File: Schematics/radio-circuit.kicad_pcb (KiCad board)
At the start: 4 copper layers, 58 x 32 mm, 40 parts, among them J1 USB_B_Micro, J2 STDC14, J3 0, U1 USBLC6-2SC6, U2 LD39015M33R, U3 STM32F042C6T6, U4 Si4705-D60-GM, Y1 SG-3030CM

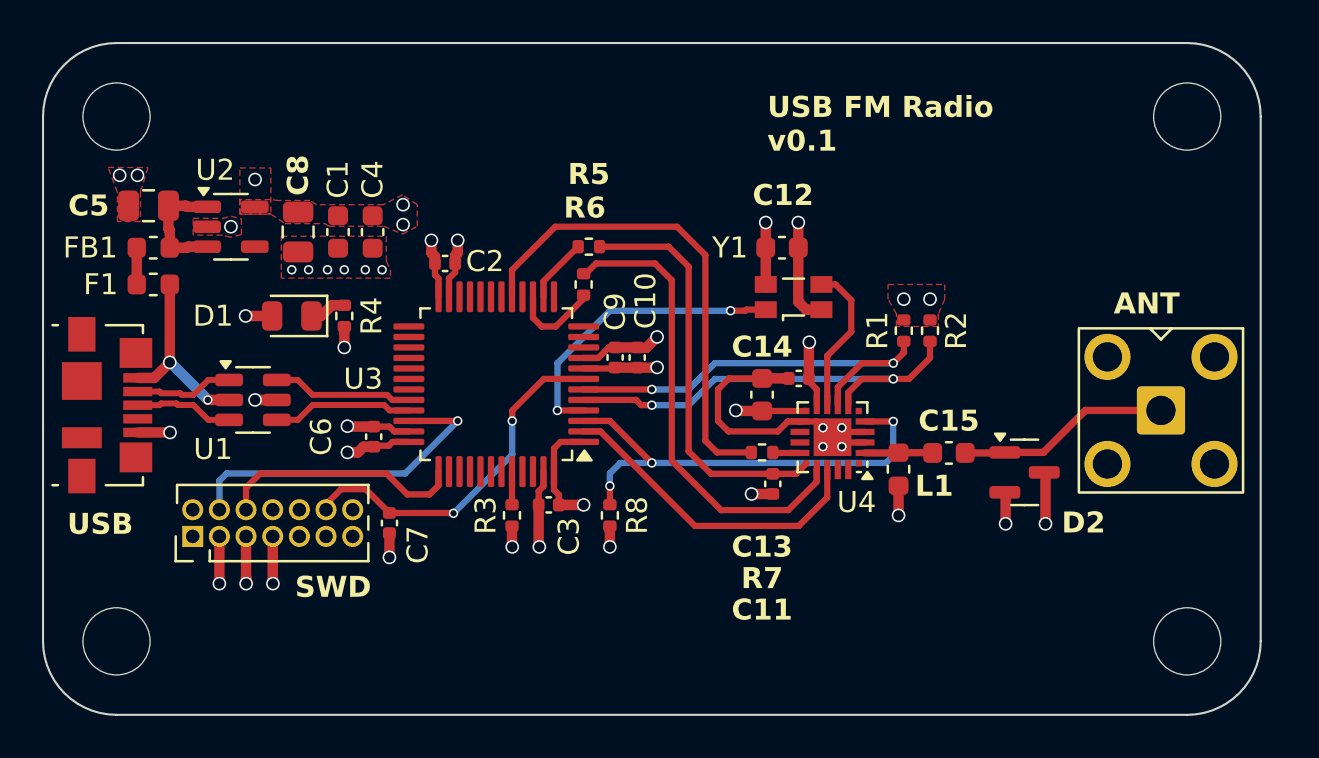
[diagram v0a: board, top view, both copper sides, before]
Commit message: Added v0.2 schematic, removed deprecation
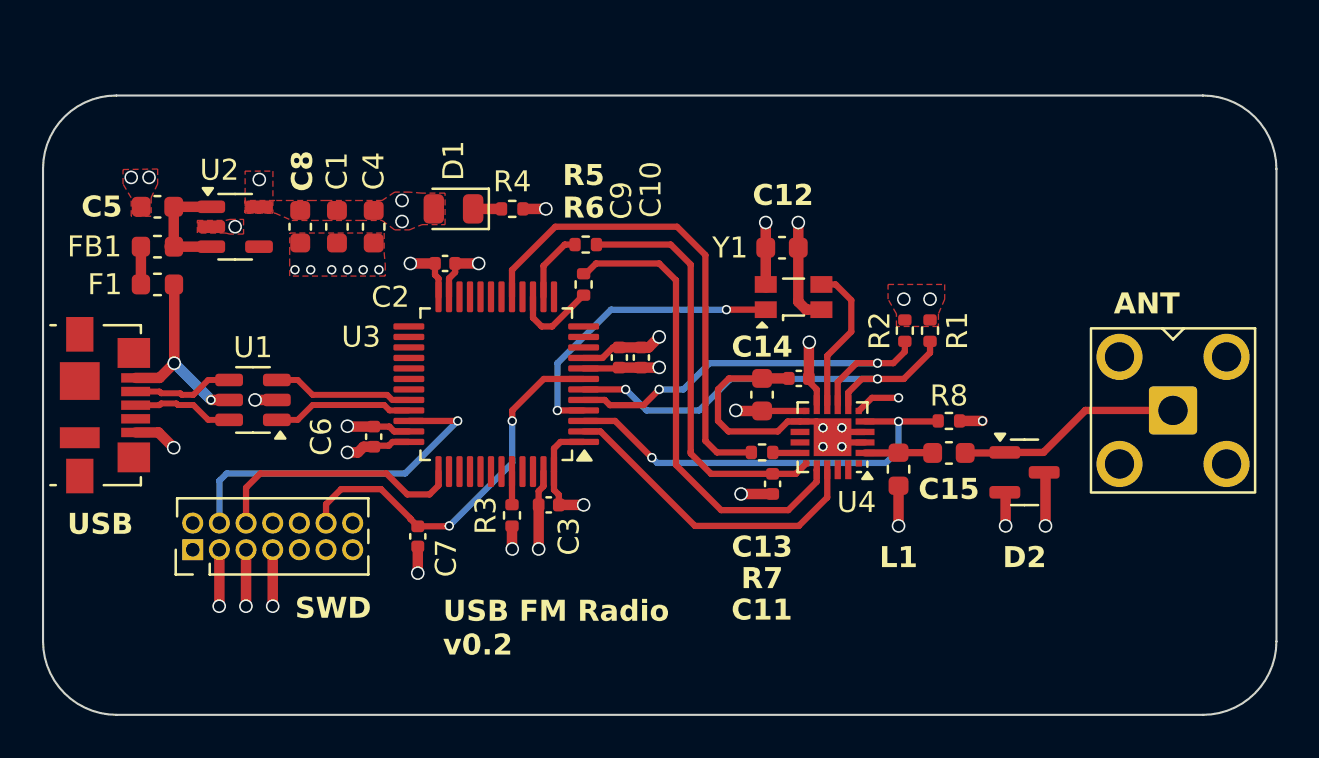
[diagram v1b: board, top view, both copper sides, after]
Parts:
- removed H1, H2, H3, H4: MountingHole, MountingHole:MountingHole_3.2mm_M3_ISO7380
- C5, C8: value 10u -> 4.7u; footprint Capacitor_SMD:C_0805_2012Metric -> Capacitor_SMD:C_0603_1608Metric
- moved R8 16.8 mm to (205.4, 125.5), turned to 180 degrees
- moved R4 9.49 mm to (184.6, 115.4), turned to 0 degrees
- moved D1 9.24 mm to (181.8, 115.4)
- moved C7 1.49 mm to (180.1, 131.0)
- moved R1 1.25 mm to (204.5, 121.2)
- moved R2 1.20 mm to (203.3, 121.2)
- moved J2 0.63 mm to (169.4, 131.6)
- moved J3 0.57 mm to (216.1, 125.0)
- moved C5 0.43 mm to (167.7, 115.3)
- moved C8 0.27 mm to (174.5, 116.2)
- moved C1 0.25 mm to (176.2, 116.2)
- moved C4 0.25 mm to (178.0, 116.2)
- moved FB1 0.21 mm to (167.7, 117.2)
- moved U2 0.20 mm to (171.4, 116.2)
- moved C10 0.20 mm to (190.8, 122.5)
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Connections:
- R1 pad 2: I2C_SDA -> I2C_SCL
- R2 pad 2: I2C_SCL -> I2C_SDA
- U1 pad 1: /USB_CONN_D- -> USB_D+
- U1 pad 2: VBUS -> GND
- U1 pad 3: /USB_CONN_D+ -> USB_D-
- U1 pad 4: USB_D+ -> /USB_CONN_D-
- U1 pad 5: GND -> VBUS
- U1 pad 6: USB_D- -> /USB_CONN_D+
- U3 pad 5: I2C_SCL -> I2C_SDA
- U3 pad 6: I2C_SDA -> I2C_SCL
- U4 pad 6: unconnected-(U4-~{SEN}-Pad6) -> GND
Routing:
- net GND: track 48.6 -> 53.7 mm, vias 30 -> 31
- net NRST: track 17.2 -> 18.6 mm
- net ~{RST}: track 22.2 -> 21.0 mm, vias 3 -> 2
- net SWCLK: track 11.8 -> 12.4 mm
- net SWDIO: track 16.2 -> 16.9 mm
- net +3.3V: track 28.1 -> 27.5 mm, vias 14 -> 13
- net /ANT: track 10.2 -> 10.7 mm
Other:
- board size 58 x 32 mm -> 58.8 x 29.5 mm
- board text added: "USB FM Radio v0.2"
- board text removed: "USB FM Radio v0.1"
